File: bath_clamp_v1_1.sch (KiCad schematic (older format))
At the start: 57 parts, among them J1 105-1103-001, J2 105-1103-001, J3 105-1103-001, K1 1462042-8, K2 1462042-8, Q1 MBT3904DW1T1G, Q3 MBT3904DW1T1G, Q4 MBT3904DW1T1G, U1 OPA828, U12 TCA9555DBR, U13 TCA9555DBR, U2 ADG1208, U3 G6L-1F-TR-DC5, U4 G6L-1F-TR-DC5, U5 G6L-1F-TR-DC5

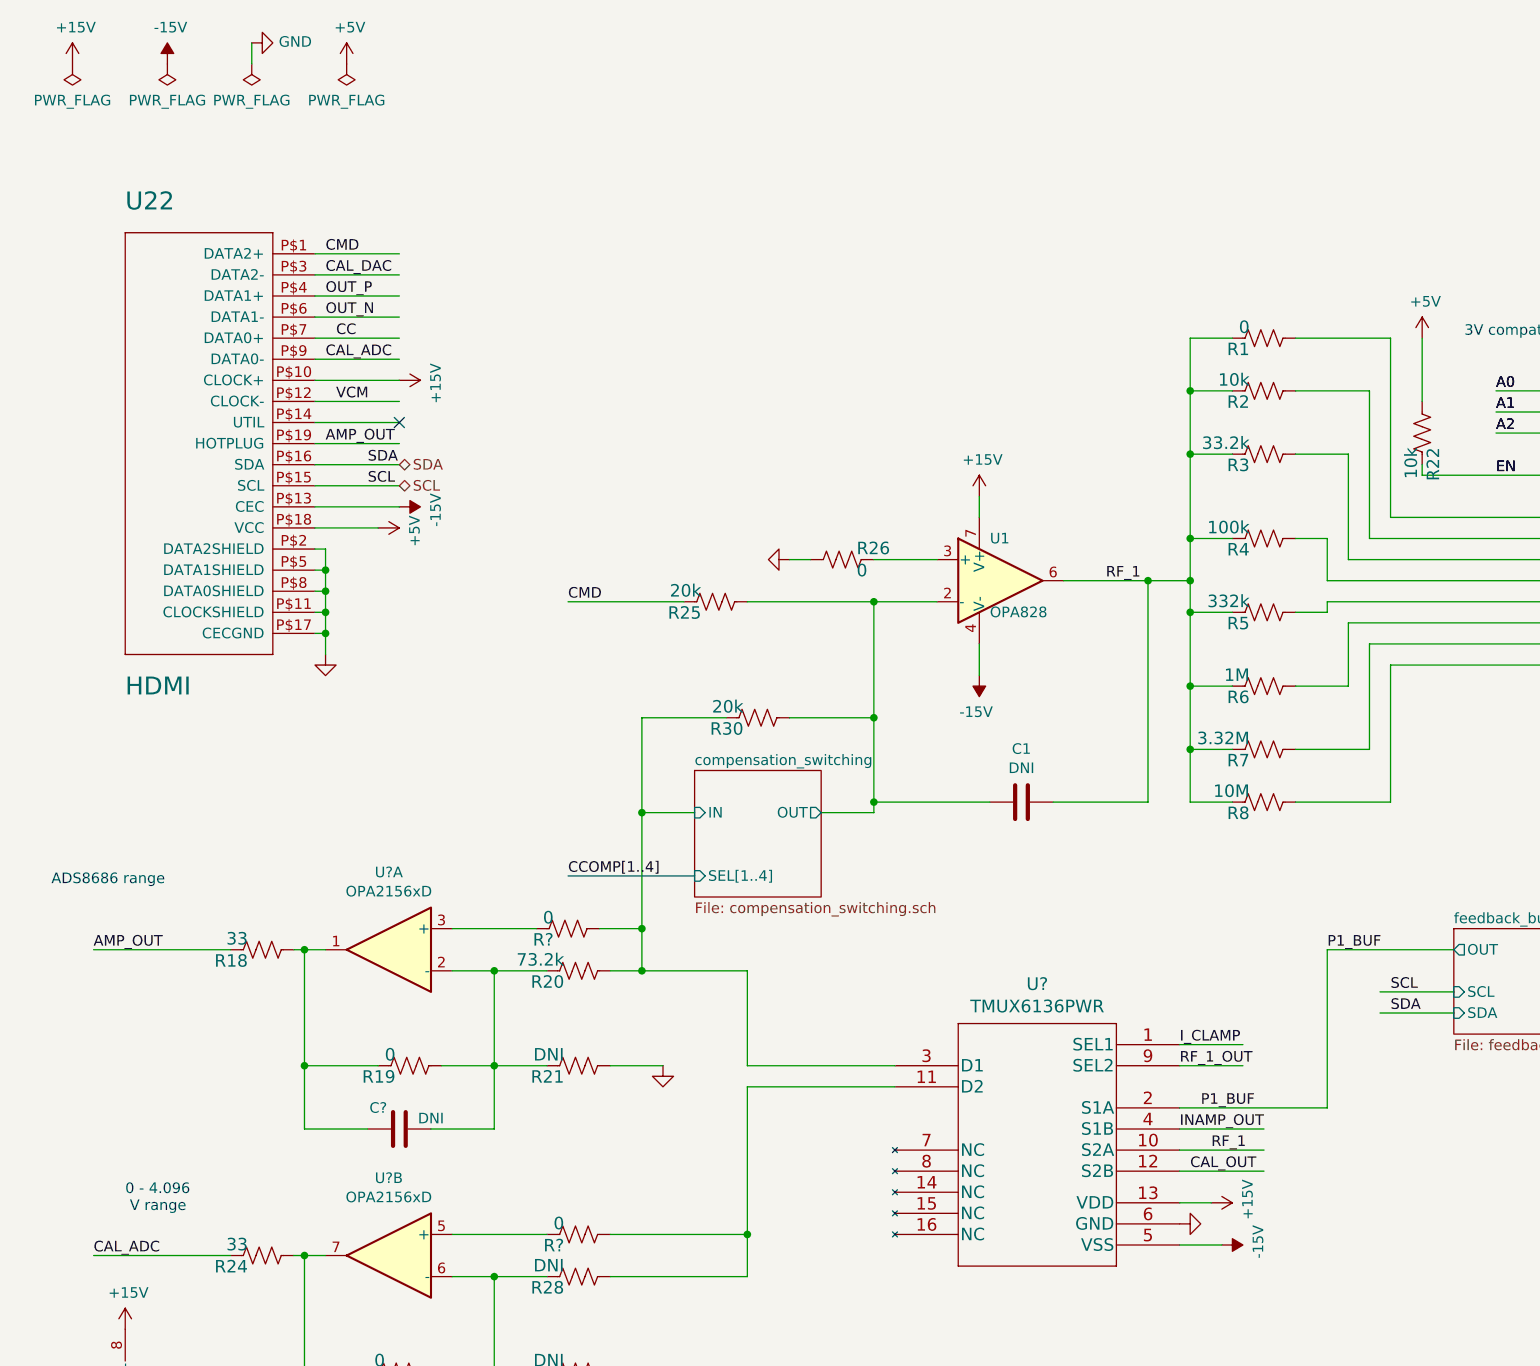
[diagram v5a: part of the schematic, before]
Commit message: updates to README
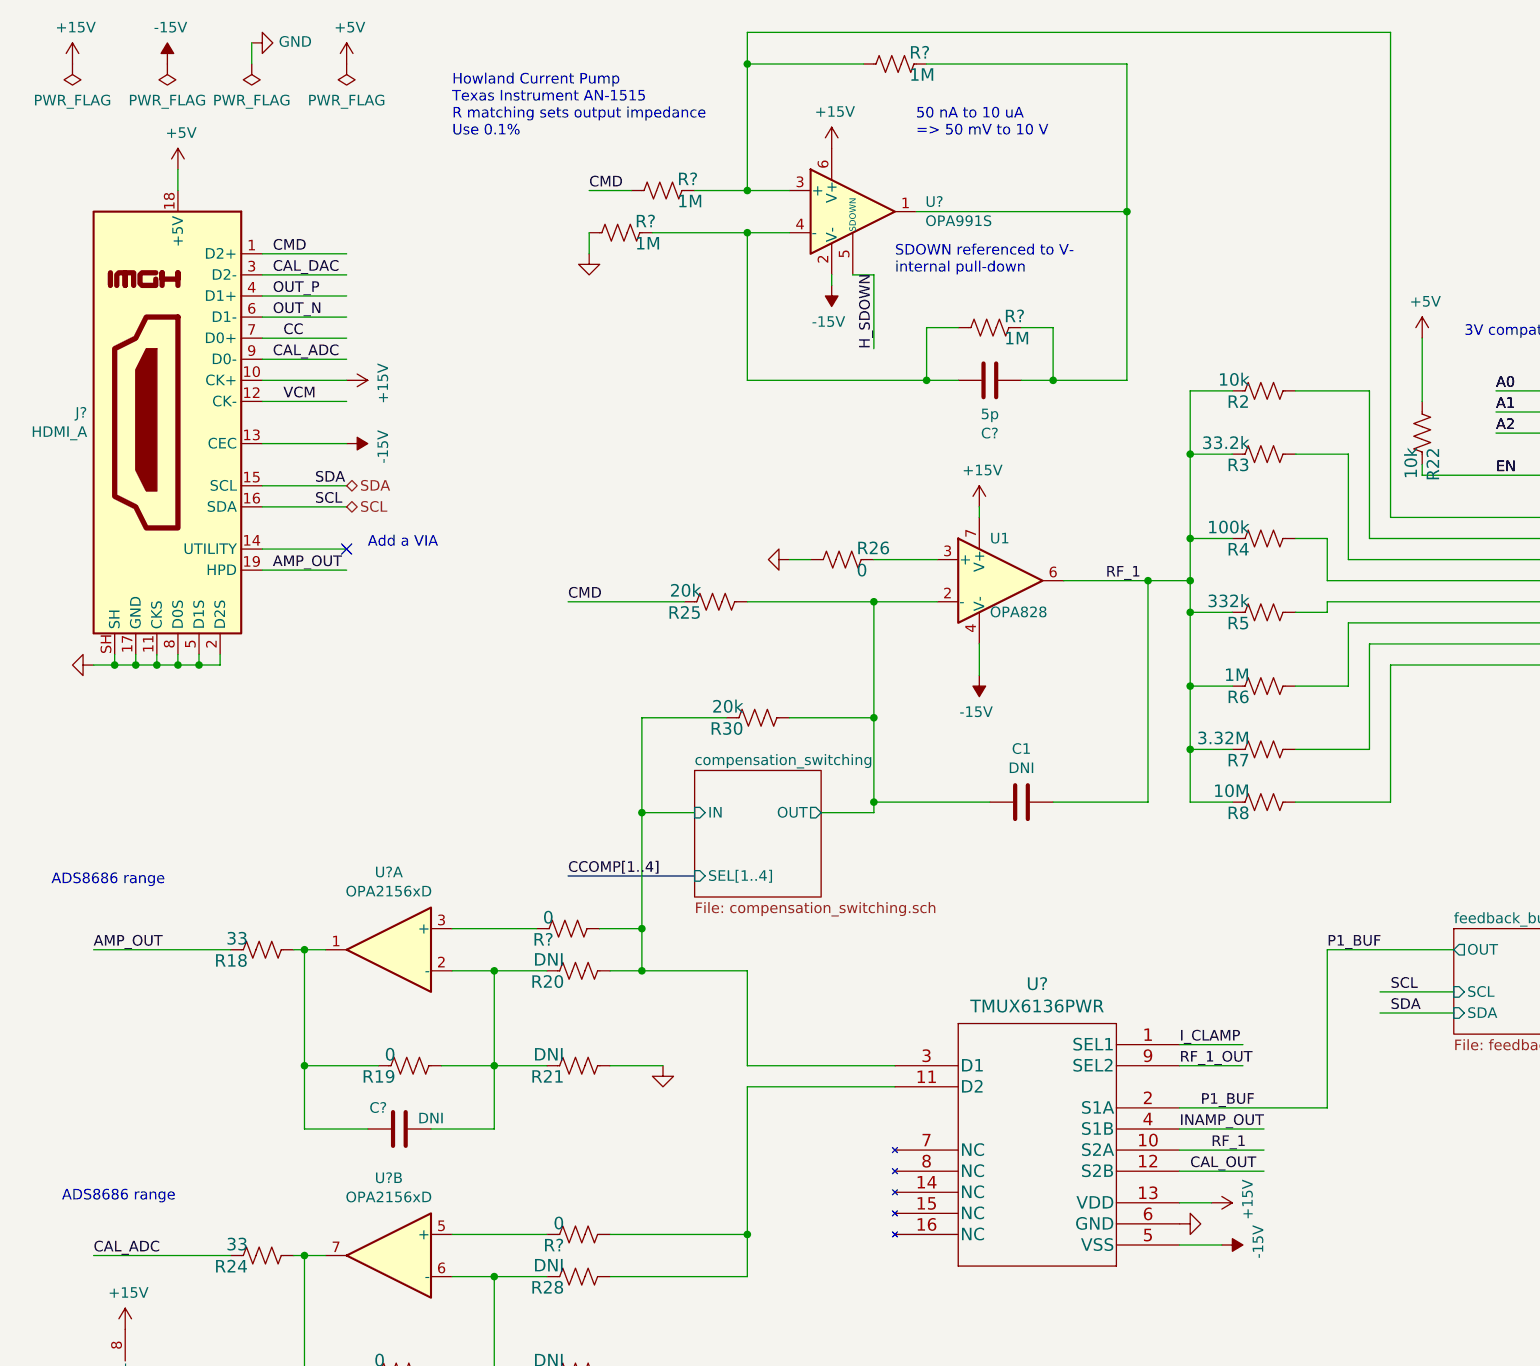
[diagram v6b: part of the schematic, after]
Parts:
- removed R1: 0, Resistor_SMD:R_0603_1608Metric, symbol Device:R_US
- removed U$2: HDMI, bath_clamp_v1:HDMI_A, symbol covg-kicad:HDMI
- added C?: 5p, Capacitor_SMD:C_0603_1608Metric, symbol Device:C
- added J?: HDMI_A, symbol Connector:HDMI_A
- added R? (x4): 1M, Resistor_SMD:R_0603_1608Metric, symbol Device:R_US
- added U?: OPA991S, Package_TO_SOT_SMD:SOT-23-6, symbol covg-kicad:OPA991S
- R20: value 73.2k -> DNI; Manf# RC0603FR-0773K2L -> (none)
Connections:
- net labels added: H_SDOWN
- wire segments 316 -> 341
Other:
- note added: "50 nA to 10 uA\n=> 50 mV to 10 V"
- note added: "Add a VIA"
- note added: "Howland Current Pump\nTexas Instrument AN-1515\nR matching sets output impedance\nUse 0.1%"
- note added: "SDOWN referenced to V-\ninternal pull-down\n"
- note removed: "0 - 4.096\n V range"

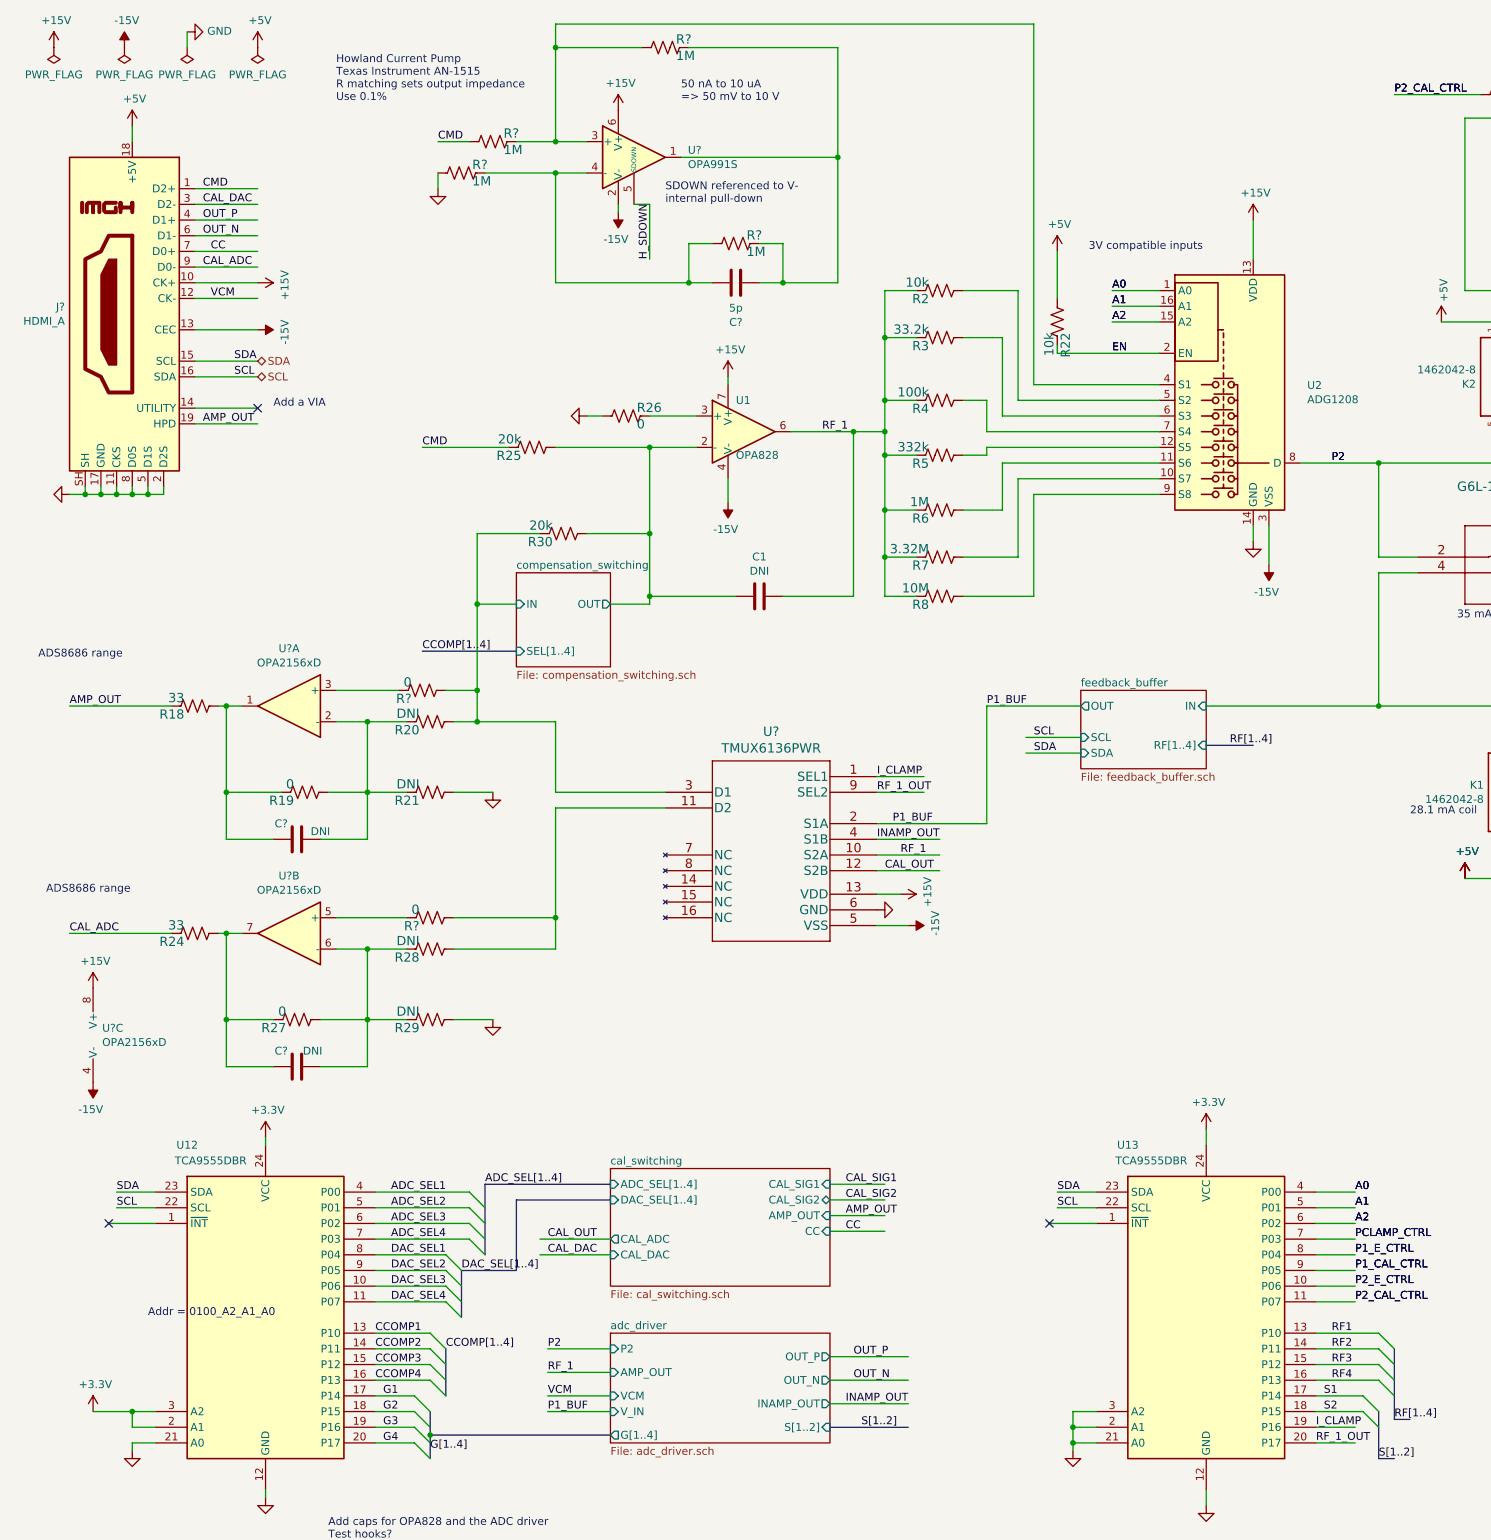
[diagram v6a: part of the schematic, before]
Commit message: update MUX for adc driver
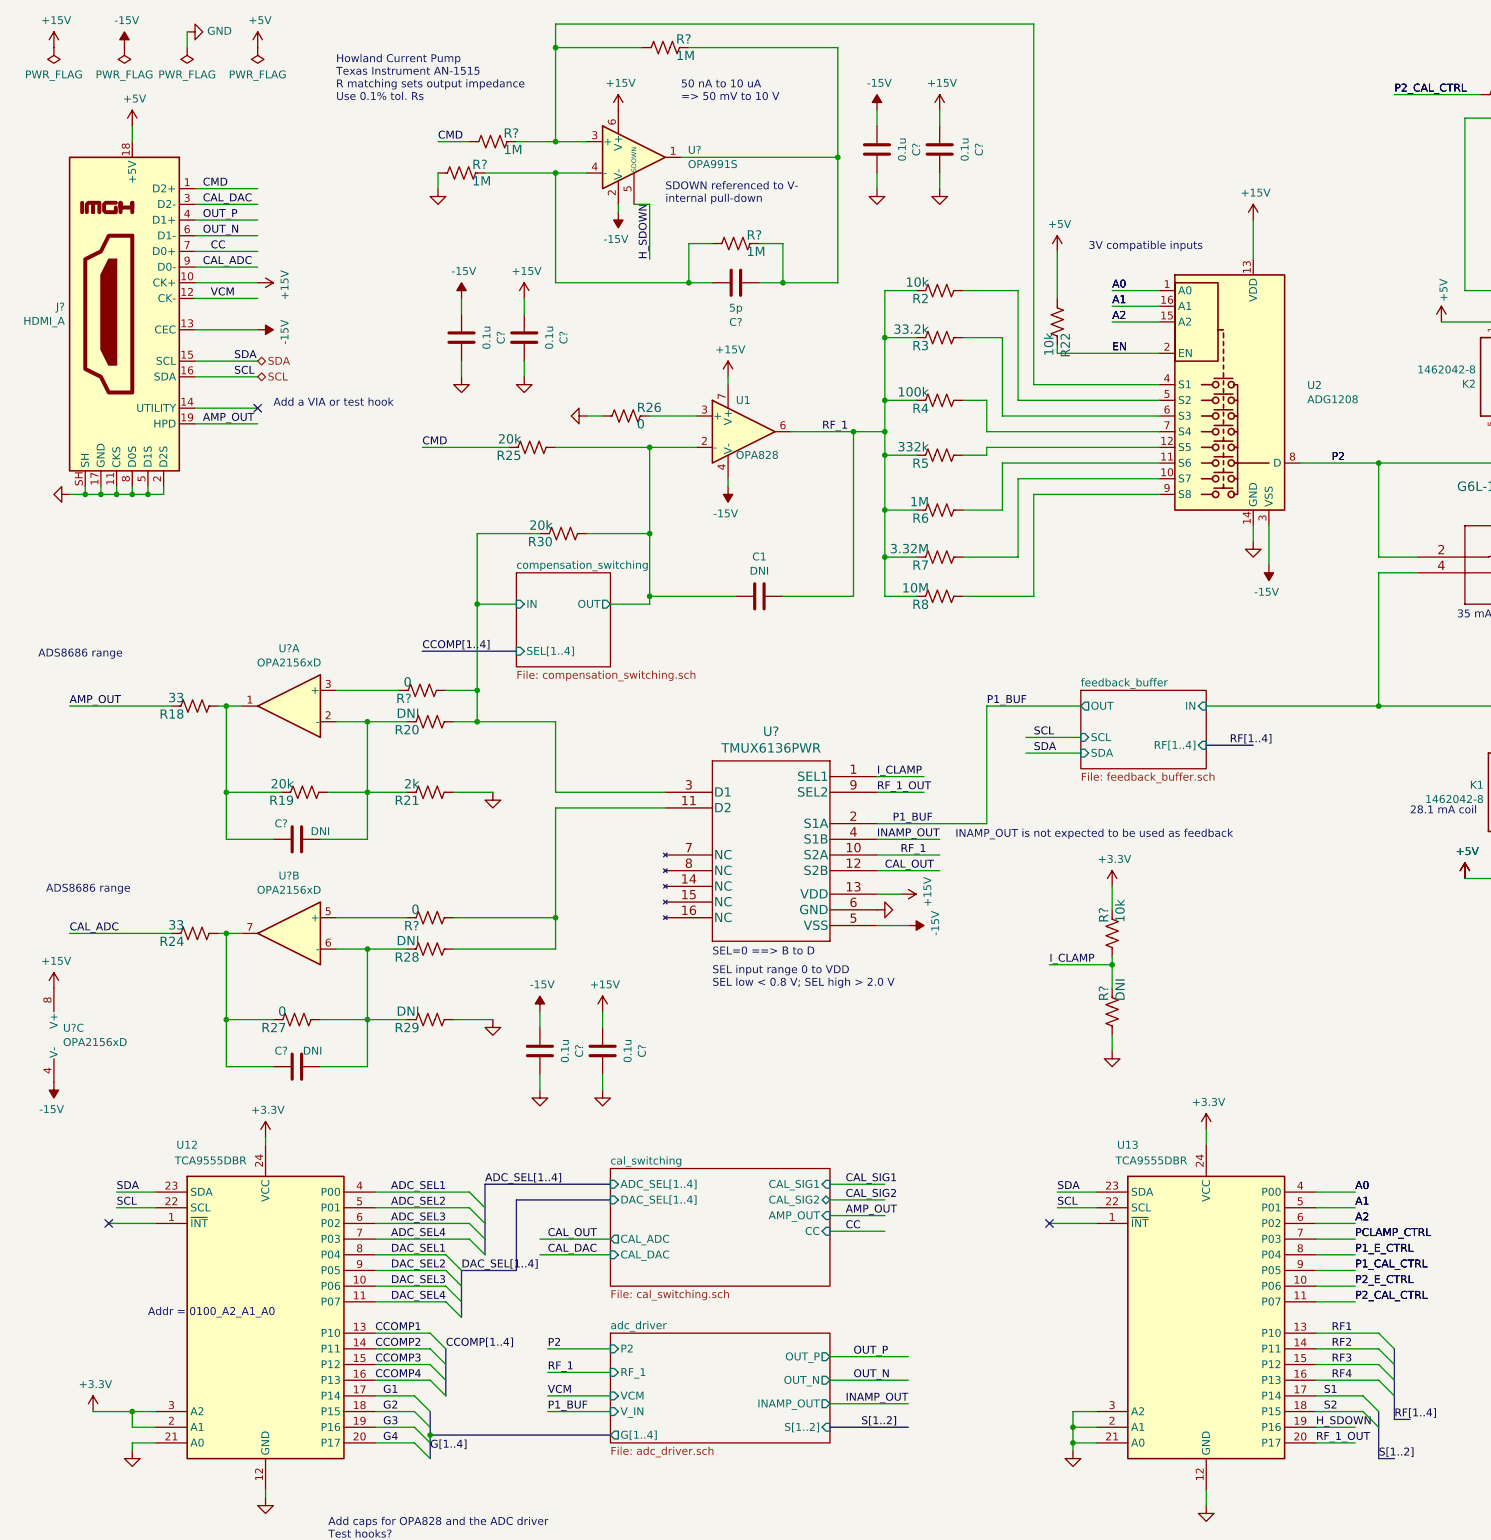
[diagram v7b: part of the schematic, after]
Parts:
- added C? (x6): 0.1u, Capacitor_SMD:C_0603_1608Metric, symbol Device:C
- added R?: 10k, Resistor_SMD:R_0603_1608Metric, symbol Device:R_US
- added R?: DNI, Resistor_SMD:R_0603_1608Metric, symbol Device:R_US
- R19: value 0 -> 20k; Manf# RC0603FR-070RL -> (none)
- R21: value DNI -> 2k
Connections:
- wire segments 341 -> 358
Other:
- note added: "Add a VIA or test hook"
- note added: "Howland Current Pump\nTexas Instrument AN-1515\nR matching sets output impedance\nUse 0.1% tol. Rs"
- note added: "INAMP_OUT is not expected to be used as feedback\n"
- note added: "SEL input range 0 to VDD\nSEL low < 0.8 V; SEL high > 2.0 V"
- note added: "SEL=0 ==> B to D"
- note removed: "Add a VIA"
- note removed: "Howland Current Pump\nTexas Instrument AN-1515\nR matching sets output impedance\nUse 0.1%"
- moved on the sheet: U?C
